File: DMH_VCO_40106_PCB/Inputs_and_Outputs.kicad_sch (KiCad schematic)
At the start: 19 parts, among them J1 TS_Jack_6.35mm_Sw, J11 Conn_01x01, J12 Conn_01x01, J150 Conn_01x12, J2 TS_Jack_6.35mm_Sw, J200 IDC_02x05, J3 TS_Jack_6.35mm_Sw, J4 TS_Jack_6.35mm_Sw, J5 TS_Jack_6.35mm_Sw, J6 TS_Jack_6.35mm_Sw, J7 TS_Jack_6.35mm_Sw, J8 TS_Jack_6.35mm_Sw, J9 TS_Jack_6.35mm_Sw, SW1 SW_SPDT_321_OnOff, SW2 SW_SPDT_321_OnOff, U7 TL071

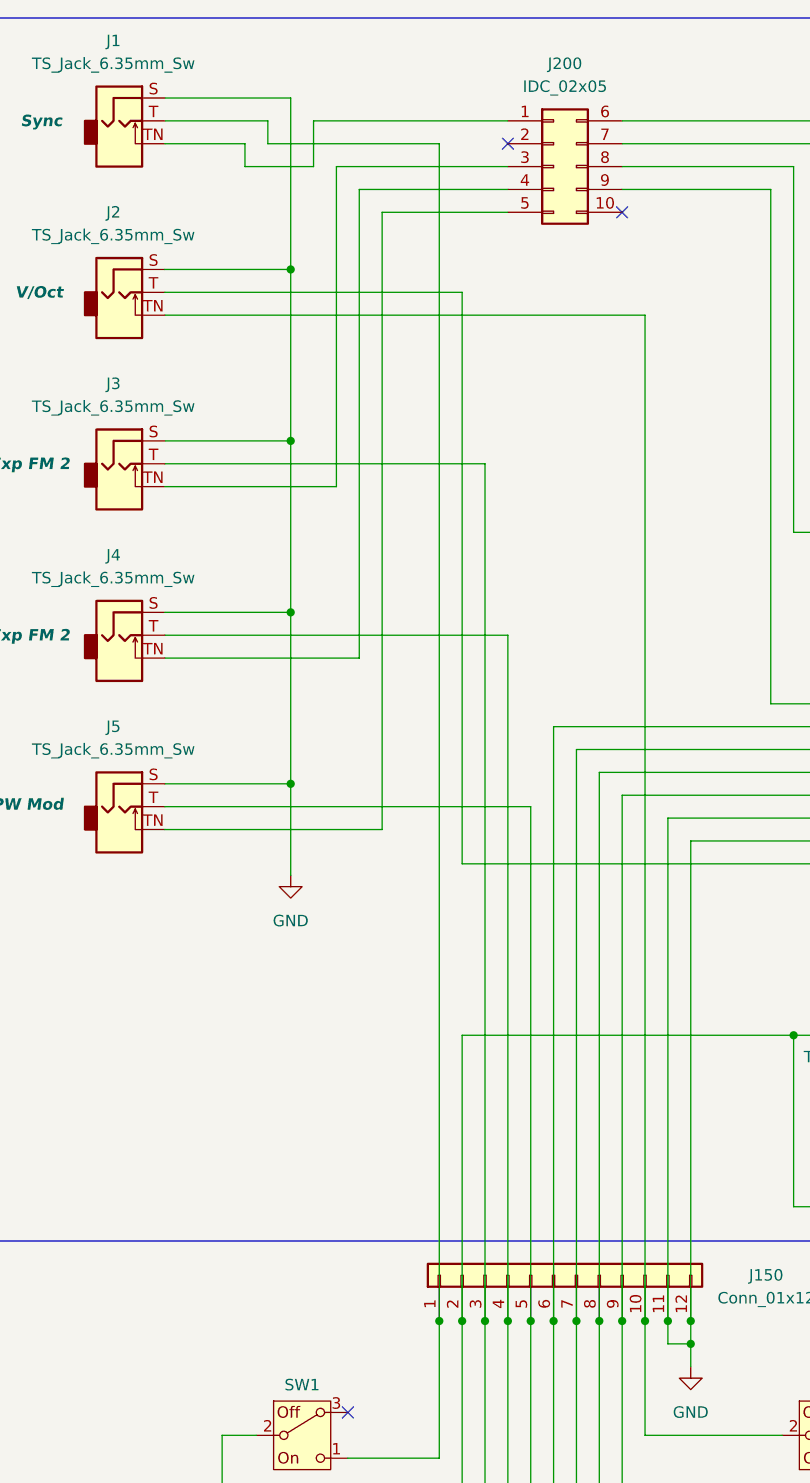
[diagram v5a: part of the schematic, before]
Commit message: Added GND to J200
... which means J2, J3 and J4 connections had to change pins.
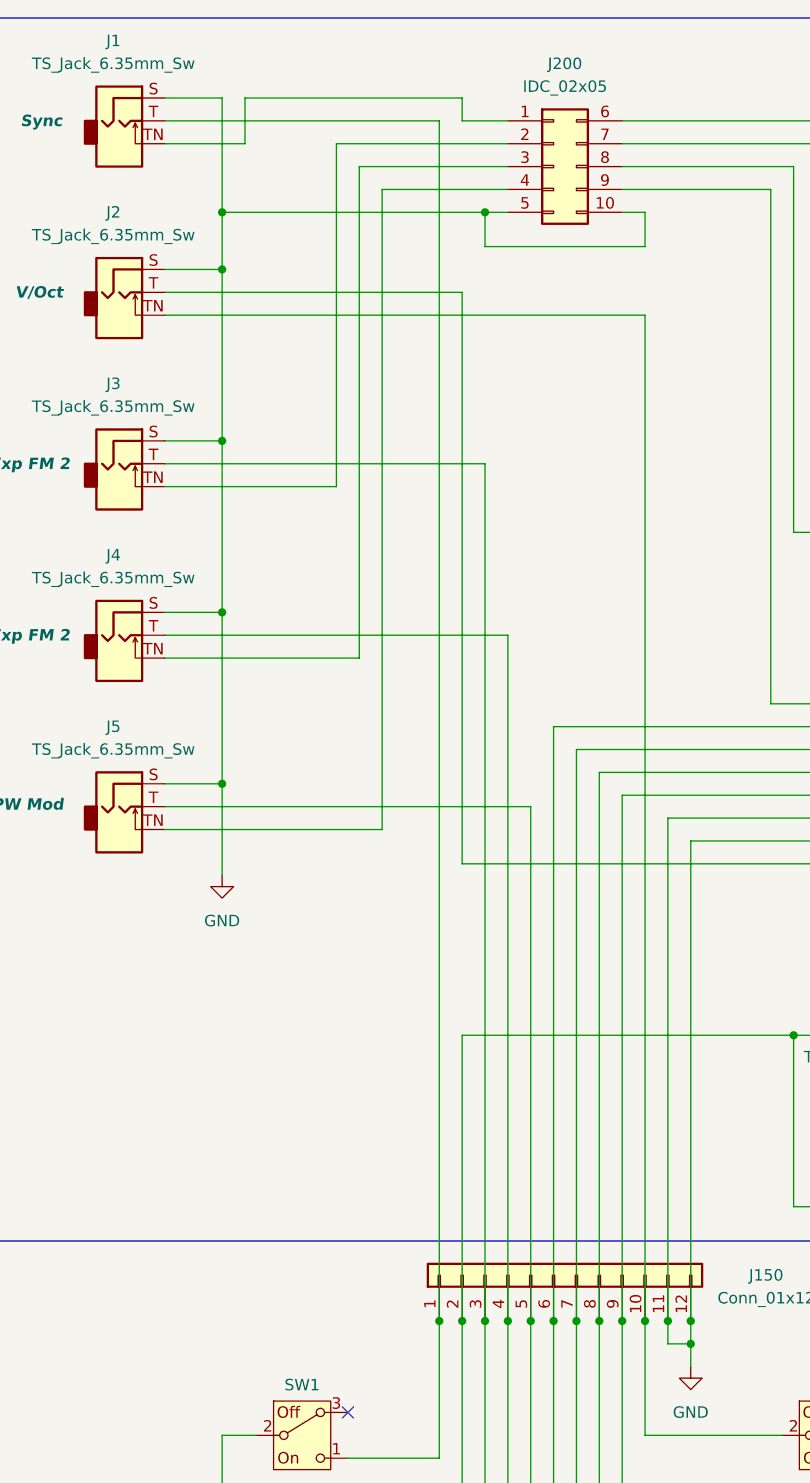
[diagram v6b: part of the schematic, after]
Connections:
- net GND: now also J200.10 (Pin_10), J200.5 (Pin_5)
- net at J3.TN: now also J200.2 (Pin_2); no longer J200.3 (Pin_3)
- net at J4.TN: now also J200.3 (Pin_3); no longer J200.4 (Pin_4)
- net at J5.TN: now also J200.4 (Pin_4); no longer J200.5 (Pin_5)
- no-connect marks 6 -> 4
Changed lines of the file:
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@@
+	)
+	(junction
+		(at 76.2 35.56)
+		(diameter 0)
+		(color 0 0 0 0)
 	)
 	(junction
@@
 	)
 	(junction
-		(at 83.82 99.06)
+		(at 76.2 99.06)
 		(diameter 0)
 		(color 0 0 0 0)
@@
 	)
 	(junction
-		(at 83.82 80.01)
+		(at 76.2 80.01)
 		(diameter 0)
 		(color 0 0 0 0)
@@
 	)
 	(junction
-		(at 83.82 60.96)
+		(at 76.2 60.96)
+		(diameter 0)
+		(color 0 0 0 0)
+	)
+	(junction
+		(at 105.41 35.56)
 		(diameter 0)
 		(color 0 0 0 0)
@@
 	)
 	(junction
-		(at 83.82 41.91)
+		(at 76.2 41.91)
 		(diameter 0)
 		(color 0 0 0 0)
@@
 		(at 148.59 168.91)
 	)
-	(no_connect
-		(at 107.95 27.94)
-	)
-	(no_connect
-		(at 120.65 35.56)
-	)
 	(wire
 		(pts
@@
 	(wire
 		(pts
-			(xy 107.95 35.56) (xy 93.98 35.56)
-		)
-		(stroke
-			(width 0)
-			(type default)
-		)
-	)
-	(wire
-		(pts
 			(xy 170.18 135.89) (xy 173.99 135.89)
 		)
@@
 	(wire
 		(pts
+			(xy 107.95 30.48) (xy 91.44 30.48)
+		)
+		(stroke
+			(width 0)
+			(type default)
+		)
+	)
+	(wire
+		(pts
 			(xy 118.11 185.42) (xy 118.11 158.75)
 		)
@@
 	(wire
 		(pts
-			(xy 83.82 99.06) (xy 83.82 109.22)
-		)
-		(stroke
-			(width 0)
-			(type default)
-		)
-	)
-	(wire
-		(pts
-			(xy 81.28 27.94) (xy 81.28 25.4)
-		)
-		(stroke
-			(width 0)
-			(type default)
-		)
-	)
-	(wire
-		(pts
-			(xy 86.36 25.4) (xy 107.95 25.4)
+			(xy 76.2 99.06) (xy 76.2 109.22)
 		)
 		(stroke
@@
 	(wire
 		(pts
-			(xy 107.95 33.02) (xy 91.44 33.02)
-		)
-		(stroke
-			(width 0)
-			(type default)
-		)
-	)
-	(wire
-		(pts
 			(xy 66.04 185.42) (xy 105.41 185.42)
 		)
@@
 	(wire
 		(pts
+			(xy 102.87 22.86) (xy 102.87 25.4)
+		)
+		(stroke
+			(width 0)
+			(type default)
+		)
+	)
+	(wire
+		(pts
 			(xy 179.07 85.09) (xy 179.07 90.17)
 		)
@@
 	(wire
 		(pts
-			(xy 78.74 30.48) (xy 78.74 27.94)
+			(xy 78.74 22.86) (xy 78.74 27.94)
 		)
 		(stroke
@@
 	(wire
 		(pts
+			(xy 76.2 35.56) (xy 105.41 35.56)
+		)
+		(stroke
+			(width 0)
+			(type default)
+		)
+	)
+	(wire
+		(pts
 			(xy 190.5 124.46) (xy 190.5 129.54)
 		)
@@
 	(wire
 		(pts
-			(xy 69.85 99.06) (xy 83.82 99.06)
+			(xy 69.85 99.06) (xy 76.2 99.06)
 		)
 		(stroke
@@
 	(wire
 		(pts
+			(xy 107.95 33.02) (xy 93.98 33.02)
+		)
+		(stroke
+			(width 0)
+			(type default)
+		)
+	)
+	(wire
+		(pts
+			(xy 93.98 33.02) (xy 93.98 104.14)
+		)
+		(stroke
+			(width 0)
+			(type default)
+		)
+	)
+	(wire
+		(pts
 			(xy 123.19 46.99) (xy 123.19 158.75)
 		)
@@
 	(wire
 		(pts
-			(xy 91.44 33.02) (xy 91.44 85.09)
+			(xy 91.44 30.48) (xy 91.44 85.09)
 		)
 		(stroke
@@
 	(wire
 		(pts
+			(xy 107.95 27.94) (xy 88.9 27.94)
+		)
+		(stroke
+			(width 0)
+			(type default)
+		)
+	)
+	(wire
+		(pts
 			(xy 137.16 33.02) (xy 137.16 90.17)
 		)
@@
 	(wire
 		(pts
-			(xy 100.33 27.94) (xy 100.33 158.75)
+			(xy 100.33 25.4) (xy 100.33 158.75)
+		)
+		(stroke
+			(width 0)
+			(type default)
+		)
+	)
+	(wire
+		(pts
+			(xy 105.41 35.56) (xy 107.95 35.56)
 		)
 		(stroke
@@
 	(wire
 		(pts
-			(xy 83.82 41.91) (xy 83.82 60.96)
+			(xy 76.2 41.91) (xy 76.2 60.96)
 		)
 		(stroke
@@
 	(wire
 		(pts
-			(xy 69.85 60.96) (xy 83.82 60.96)
+			(xy 88.9 27.94) (xy 88.9 66.04)
+		)
+		(stroke
+			(width 0)
+			(type default)
+		)
+	)
+	(wire
+		(pts
+			(xy 69.85 60.96) (xy 76.2 60.96)
 		)
 		(stroke
@@
 	(wire
 		(pts
-			(xy 93.98 35.56) (xy 93.98 104.14)
-		)
-		(stroke
-			(width 0)
-			(type default)
-		)
-	)
-	(wire
-		(pts
 			(xy 88.9 66.04) (xy 69.85 66.04)
 		)
@@
 	(wire
 		(pts
-			(xy 83.82 22.86) (xy 83.82 41.91)
+			(xy 76.2 22.86) (xy 76.2 35.56)
 		)
 		(stroke
@@
 	(wire
 		(pts
+			(xy 123.19 35.56) (xy 123.19 39.37)
+		)
+		(stroke
+			(width 0)
+			(type default)
+		)
+	)
+	(wire
+		(pts
 			(xy 181.61 25.4) (xy 181.61 92.71)
 		)
@@
 	(wire
 		(pts
-			(xy 100.33 27.94) (xy 81.28 27.94)
+			(xy 76.2 35.56) (xy 76.2 41.91)
 		)
 		(stroke
@@
 	(wire
 		(pts
+			(xy 105.41 39.37) (xy 123.19 39.37)
+		)
+		(stroke
+			(width 0)
+			(type default)
+		)
+	)
+	(wire
+		(pts
 			(xy 102.87 107.95) (xy 190.5 107.95)
 		)
@@
 	(wire
 		(pts
-			(xy 69.85 22.86) (xy 83.82 22.86)
+			(xy 69.85 22.86) (xy 76.2 22.86)
 		)
 		(stroke
@@
 	(wire
 		(pts
-			(xy 69.85 80.01) (xy 83.82 80.01)
+			(xy 69.85 80.01) (xy 76.2 80.01)
+		)
+		(stroke
+			(width 0)
+			(type default)
+		)
+	)
+	(wire
+		(pts
+			(xy 120.65 35.56) (xy 123.19 35.56)
 		)
 		(stroke
@@
 	(wire
 		(pts
-			(xy 81.28 25.4) (xy 69.85 25.4)
-		)
-		(stroke
-			(width 0)
-			(type default)
-		)
-	)
-	(wire
-		(pts
-			(xy 83.82 80.01) (xy 83.82 99.06)
+			(xy 69.85 25.4) (xy 100.33 25.4)
+		)
+		(stroke
+			(width 0)
+			(type default)
+		)
+	)
+	(wire
+		(pts
+			(xy 76.2 80.01) (xy 76.2 99.06)
 		)
 		(stroke
@@
 	(wire
 		(pts
-			(xy 69.85 41.91) (xy 83.82 41.91)
+			(xy 69.85 41.91) (xy 76.2 41.91)
 		)
 		(stroke
@@
 	(wire
 		(pts
-			(xy 83.82 60.96) (xy 83.82 80.01)
+			(xy 102.87 25.4) (xy 107.95 25.4)
+		)
+		(stroke
+			(width 0)
+			(type default)
+		)
+	)
+	(wire
+		(pts
+			(xy 76.2 60.96) (xy 76.2 80.01)
 		)
 		(stroke
@@
 	(wire
 		(pts
-			(xy 86.36 30.48) (xy 86.36 25.4)
-		)
-		(stroke
-			(width 0)
-			(type default)
-		)
-	)
-	(wire
-		(pts
 			(xy 184.15 118.11) (xy 184.15 135.89)
 		)
@@
 	(wire
 		(pts
-			(xy 107.95 30.48) (xy 88.9 30.48)
-		)
-		(stroke
-			(width 0)
-			(type default)
-		)
-	)
-	(wire
-		(pts
 			(xy 154.94 118.11) (xy 154.94 119.38)
 		)
@@
 	(wire
 		(pts
-			(xy 88.9 30.48) (xy 88.9 66.04)
-		)
-		(stroke
-			(width 0)
-			(type default)
-		)
-	)
-	(wire
-		(pts
 			(xy 152.4 177.8) (xy 156.21 177.8)
 		)
@@
 	(wire
 		(pts
-			(xy 78.74 30.48) (xy 86.36 30.48)
+			(xy 78.74 22.86) (xy 102.87 22.86)
+		)
+		(stroke
+			(width 0)
+			(type default)
+		)
+	)
+	(wire
+		(pts
+			(xy 105.41 35.56) (xy 105.41 39.37)
 		)
 		(stroke
@@
 	(symbol
 		(lib_id "power:GND")
-		(at 83.82 109.22 0)
+		(at 76.2 109.22 0)
 		(unit 1)
 		(exclude_from_sim no)
@@
 		(fields_autoplaced yes)
 		(property "Reference" "#PWR05"
-			(at 83.82 115.57 0)
+			(at 76.2 115.57 0)
 			(effects
 				(font
@@
 		)
 		(property "Value" "GND"
-			(at 83.82 114.3 0)
+			(at 76.2 114.3 0)
 			(effects
 				(font
@@
 		)
 		(property "Footprint" ""
-			(at 83.82 109.22 0)
+			(at 76.2 109.22 0)
 			(effects
 				(font
@@
 		)
 		(property "Datasheet" ""
-			(at 83.82 109.22 0)
+			(at 76.2 109.22 0)
 			(effects
 				(font
@@
 		)
 		(property "Description" "Power symbol creates a global label with name \"GND\" , ground"
-			(at 83.82 109.22 0)
-			(effects
-				(font
+			(at 76.2 109.22 0)
+			(effects
+				(font

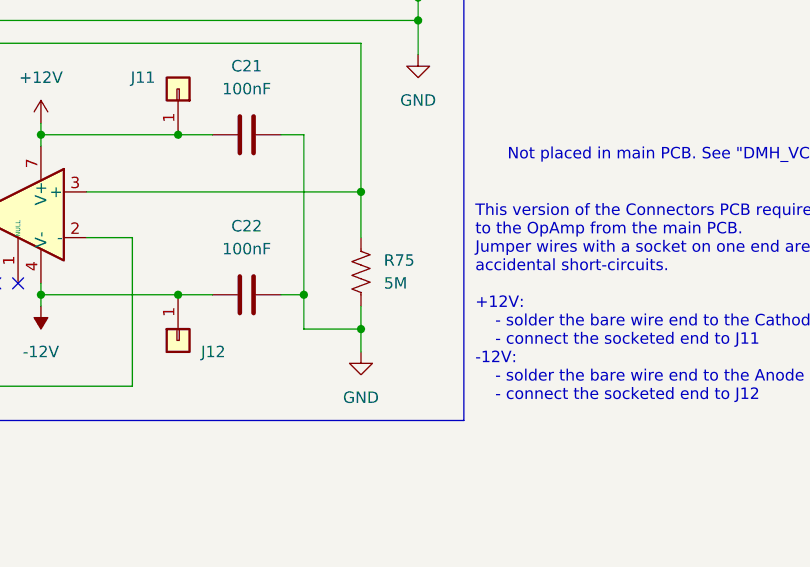
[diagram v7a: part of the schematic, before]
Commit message: Changed buffer resistor to 10M
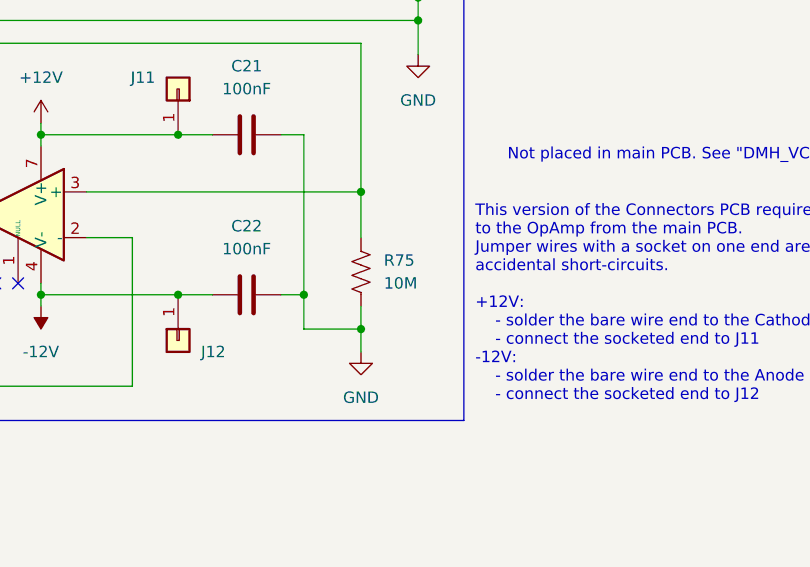
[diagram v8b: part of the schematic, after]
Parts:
- R75: value 5M -> 10M
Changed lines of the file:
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@@
 			)
 		)
-		(property "Value" "5M"
+		(property "Value" "10M"
 			(at 193.04 134.6199 0)
 			(effects
